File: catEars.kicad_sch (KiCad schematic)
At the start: 32 parts, among them J1 Conn_01x03_Socket, J2 Conn_01x03_Socket, J3 USB_C_Receptacle_PowerOnly_6P, U1 ESP-01v090, U2 AMS1117-3.3

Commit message: pcb
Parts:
- removed C10, C9: 100nF, C0805, symbol Device:C
- removed D10, D9: WS2812B, LED_SMD:LED_WS2812B_PLCC4_5.0x5.0mm_P3.2mm, symbol LED:WS2812B
- removed SW1: ~, symbol Switch:SW_Push
- C1, C11, C12, C2, C3, C4, C5, C6, C7, C8: footprint C0805 -> Capacitor_SMD:C_0805_2012Metric_Pad1.18x1.45mm_HandSolder
- J1, J2: footprint (none) -> Connector_PinHeader_2.54mm:PinHeader_1x03_P2.54mm_Vertical
- R1, R2, R3, R4: footprint 0805 -> Resistor_SMD:R_0805_2012Metric_Pad1.20x1.40mm_HandSolder
- U1: footprint (none) -> ESP8266:ESP-01
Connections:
- net VCC is gone; now on net +5V: J1.2 (Pin_2), J2.2 (Pin_2)
- net LED_out: now also D8.2 (DOUT)
- no-connect marks 0 -> 2

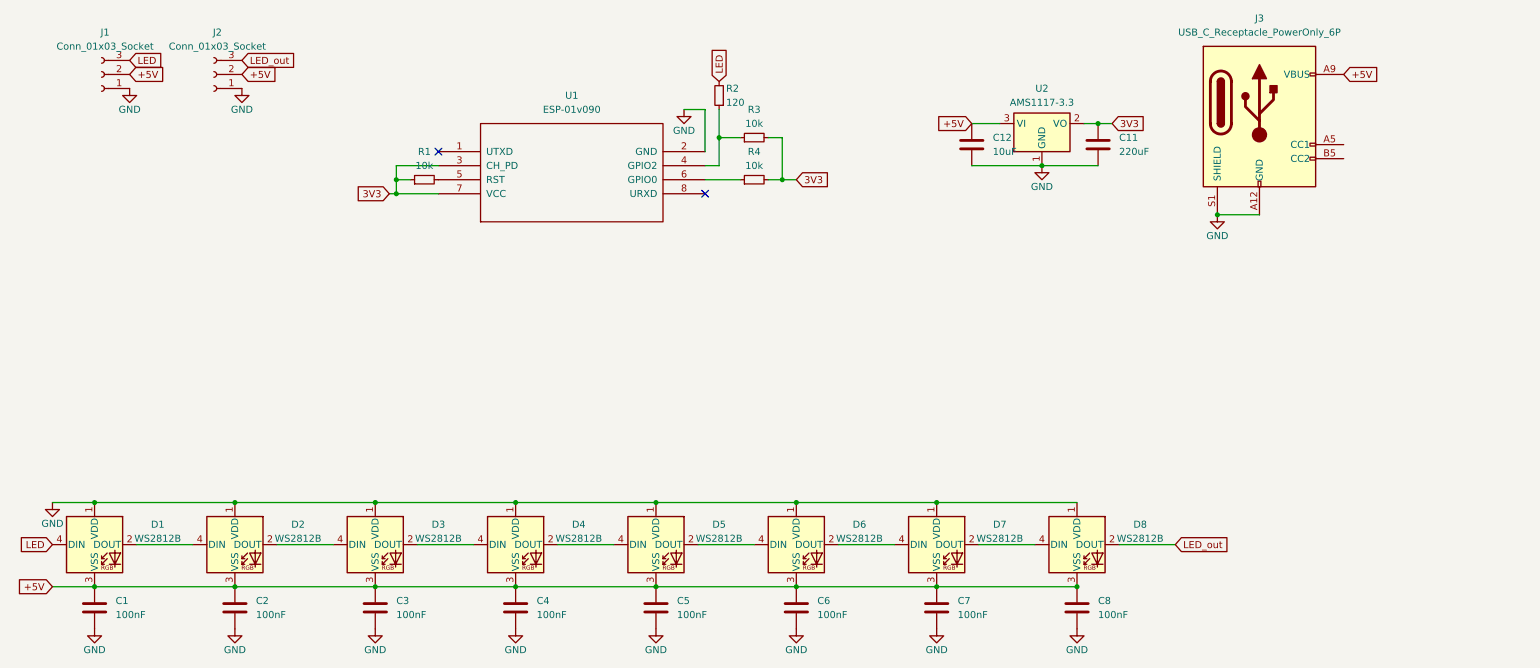
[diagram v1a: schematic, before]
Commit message: fixed WS2812 VSS VDD
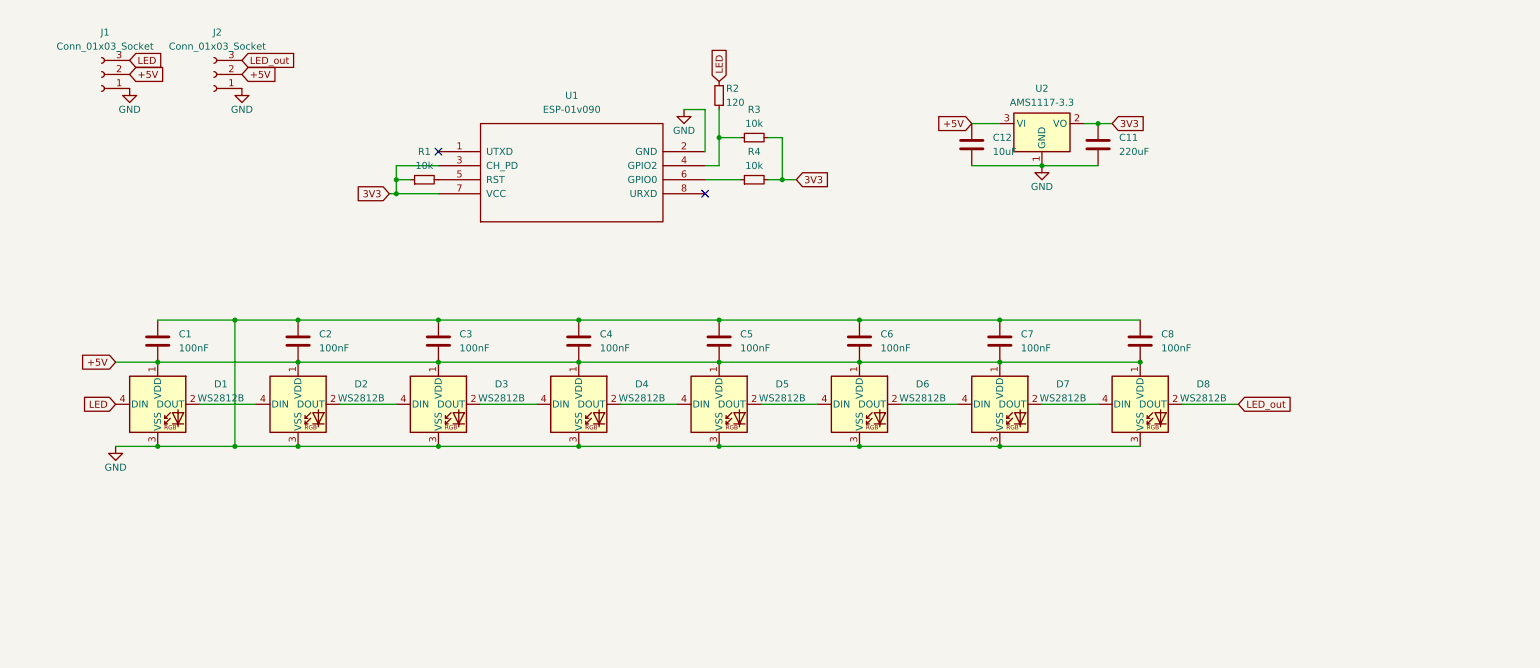
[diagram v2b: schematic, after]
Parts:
- removed J3: USB_C_Receptacle_PowerOnly_6P, symbol Connector:USB_C_Receptacle_PowerOnly_6P
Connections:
- net +5V: now also C1.2, C2.2, C3.2, C4.2, C5.2, C6.2, C7.2, C8.2, D1.1 (VDD), D2.1 (VDD), D3.1 (VDD), D4.1 (VDD), D5.1 (VDD), D6.1 (VDD), D7.1 (VDD), D8.1 (VDD); no longer C1.1, C2.1, C3.1, C4.1, C5.1, C6.1, C7.1, C8.1, D1.3 (VSS), D2.3 (VSS), D3.3 (VSS), D4.3 (VSS), D5.3 (VSS), D6.3 (VSS), D7.3 (VSS), D8.3 (VSS)
- net GND: now also C1.1, C2.1, C3.1, C4.1, C5.1, C6.1, C7.1, C8.1, D1.3 (VSS), D2.3 (VSS), D3.3 (VSS), D4.3 (VSS), D5.3 (VSS), D6.3 (VSS), D7.3 (VSS), D8.3 (VSS); no longer C1.2, C2.2, C3.2, C4.2, C5.2, C6.2, C7.2, C8.2, D1.1 (VDD), D2.1 (VDD), D3.1 (VDD), D4.1 (VDD), D5.1 (VDD), D6.1 (VDD), D7.1 (VDD), D8.1 (VDD)
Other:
- moved on the sheet: D1, D2, D3, D4, D5, D6, D7, D8

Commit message: some optimisations
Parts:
- renumbered R4 to R2, R2 to R4
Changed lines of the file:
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@@
   (symbol (lib_id "Device:R_Small") (at 139.7 33.02 180) (unit 1)
     (in_bom yes) (on_board yes) (dnp no)
-    (property "Reference" "R2" (at 140.97 31.75 0)
+    (property "Reference" "R4" (at 140.97 31.75 0)
       (effects (font (size 1.27 1.27)) (justify right))
     )
@@
       (project "catEars"
         (path "/652ac57d-1a15-486c-917b-0d768241161c"
-          (reference "R2") (unit 1)
+          (reference "R4") (unit 1)
         )
       )
@@
   (symbol (lib_id "Device:R_Small") (at 146.05 48.26 90) (unit 1)
     (in_bom yes) (on_board yes) (dnp no) (fields_autoplaced)
-    (property "Reference" "R4" (at 146.05 43.18 90)
+    (property "Reference" "R2" (at 146.05 43.18 90)
       (effects (font (size 1.27 1.27)))
     )
@@
       (project "catEars"
         (path "/652ac57d-1a15-486c-917b-0d768241161c"
-          (reference "R4") (unit 1)
+          (reference "R2") (unit 1)
         )
       )

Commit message: changed R12 value
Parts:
- C12: value 10uF -> 22uF
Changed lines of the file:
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@@
       (effects (font (size 1.27 1.27)) (justify left))
     )
-    (property "Value" "10uF" (at 189.23 43.18 0)
+    (property "Value" "22uF" (at 189.23 43.18 0)
       (effects (font (size 1.27 1.27)) (justify left))
     )

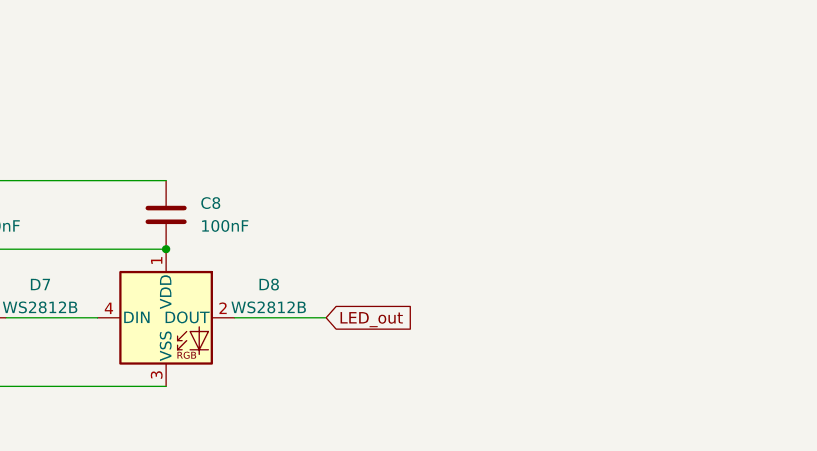
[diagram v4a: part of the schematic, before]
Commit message: added 2 leds in schematic
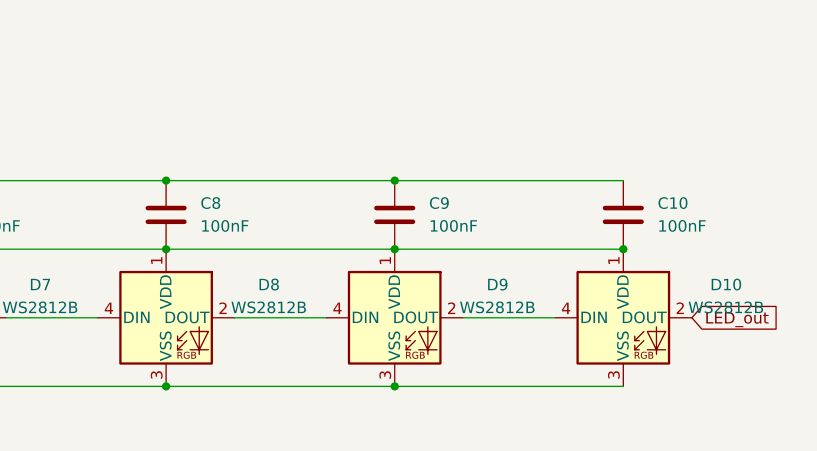
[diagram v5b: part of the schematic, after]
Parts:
- added C10, C9: 100nF, Capacitor_SMD:C_0805_2012Metric_Pad1.18x1.45mm_HandSolder, symbol Device:C
- added D10, D9: WS2812B, LED_SMD:LED_WS2812B_PLCC4_5.0x5.0mm_P3.2mm, symbol LED:WS2812B
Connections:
- net +5V: now also C10.2, C9.2, D10.1 (VDD), D9.1 (VDD)
- net GND: now also C10.1, C9.1, D10.3 (VSS), D9.3 (VSS)
- net LED_out: now also D10.2 (DOUT); no longer D8.2 (DOUT)
- new net: D8.2 (DOUT), D9.4 (DIN)
- new net: D10.4 (DIN), D9.2 (DOUT)
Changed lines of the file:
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@@
   (junction (at 114.3 96.52) (diameter 0) (color 0 0 0 0)
   )
+  (junction (at 241.3 96.52) (diameter 0) (color 0 0 0 0)
+  )
   (junction (at 38.1 96.52) (diameter 0) (color 0 0 0 0)
   )
@@
   (junction (at 139.7 96.52) (diameter 0) (color 0 0 0 0)
   )
+  (junction (at 215.9 96.52) (diameter 0) (color 0 0 0 0)
+  )
   (junction (at 52.07 96.52) (diameter 0) (color 0 0 0 0)
   )
+  (junction (at 88.9 96.52) (diameter 0) (color 0 0 0 0)
+  )
+  (junction (at 63.5 96.52) (diameter 0) (color 0 0 0 0)
+  )
+  (junction (at 139.7 73.66) (diameter 0) (color 0 0 0 0)
+  )
+  (junction (at 208.28 38.1) (diameter 0) (color 194 0 0 1)
+  )
+  (junction (at 198.12 45.72) (diameter 0) (color 0 0 255 1)
+  )
+  (junction (at 114.3 81.28) (diameter 0) (color 132 0 0 1)
+  )
+  (junction (at 215.9 81.28) (diameter 0) (color 0 0 0 0)
+  )
+  (junction (at 266.7 81.28) (diameter 0) (color 0 0 0 0)
+  )
+  (junction (at 63.5 73.66) (diameter 0) (color 0 0 0 0)
+  )
+  (junction (at 139.7 81.28) (diameter 0) (color 132 0 0 1)
+  )
+  (junction (at 190.5 96.52) (diameter 0) (color 0 0 0 0)
+  )
+  (junction (at 241.3 81.28) (diameter 0) (color 132 0 0 1)
+  )
+  (junction (at 165.1 96.52) (diameter 0) (color 0 0 0 0)
+  )
+  (junction (at 190.5 81.28) (diameter 0) (color 132 0 0 1)
+  )
+  (junction (at 215.9 73.66) (diameter 0) (color 0 0 0 0)
+  )
+  (junction (at 165.1 81.28) (diameter 0) (color 132 0 0 1)
+  )
+  (junction (at 139.7 40.64) (diameter 0) (color 0 0 0 0)
+  )
+  (junction (at 88.9 81.28) (diameter 0) (color 132 0 0 1)
+  )
+  (junction (at 165.1 73.66) (diameter 0) (color 0 0 0 0)
+  )
+  (junction (at 52.07 73.66) (diameter 0) (color 0 0 0 0)
+  )
+  (junction (at 241.3 73.66) (diameter 0) (color 0 0 0 0)
+  )
+  (junction (at 63.5 81.28) (diameter 0) (color 132 0 0 1)
+  )
   (junction (at 190.5 73.66) (diameter 0) (color 0 0 0 0)
-  )
-  (junction (at 88.9 96.52) (diameter 0) (color 0 0 0 0)
-  )
-  (junction (at 63.5 96.52) (diameter 0) (color 0 0 0 0)
-  )
-  (junction (at 139.7 73.66) (diameter 0) (color 0 0 0 0)
-  )
-  (junction (at 208.28 38.1) (diameter 0) (color 194 0 0 1)
-  )
-  (junction (at 198.12 45.72) (diameter 0) (color 0 0 255 1)
-  )
-  (junction (at 114.3 81.28) (diameter 0) (color 132 0 0 1)
-  )
-  (junction (at 215.9 81.28) (diameter 0) (color 0 0 0 0)
-  )
-  (junction (at 63.5 73.66) (diameter 0) (color 0 0 0 0)
-  )
-  (junction (at 139.7 81.28) (diameter 0) (color 132 0 0 1)
-  )
-  (junction (at 190.5 96.52) (diameter 0) (color 0 0 0 0)
-  )
-  (junction (at 165.1 96.52) (diameter 0) (color 0 0 0 0)
-  )
-  (junction (at 190.5 81.28) (diameter 0) (color 132 0 0 1)
-  )
-  (junction (at 165.1 81.28) (diameter 0) (color 132 0 0 1)
-  )
-  (junction (at 139.7 40.64) (diameter 0) (color 0 0 0 0)
-  )
-  (junction (at 88.9 81.28) (diameter 0) (color 132 0 0 1)
-  )
-  (junction (at 165.1 73.66) (diameter 0) (color 0 0 0 0)
-  )
-  (junction (at 52.07 73.66) (diameter 0) (color 0 0 0 0)
-  )
-  (junction (at 63.5 81.28) (diameter 0) (color 132 0 0 1)
   )
   (junction (at 88.9 73.66) (diameter 0) (color 0 0 0 0)
@@
     (stroke (width 0) (type default) (color 194 0 0 1))
   )
+  (wire (pts (xy 215.9 81.28) (xy 241.3 81.28))
+    (stroke (width 0) (type default) (color 132 0 0 1))
+  )
   (wire (pts (xy 139.7 45.72) (xy 137.16 45.72))
+    (stroke (width 0) (type default))
+  )
+  (wire (pts (xy 190.5 73.66) (xy 215.9 73.66))
     (stroke (width 0) (type default))
   )
@@
     (stroke (width 0) (type default))
   )
+  (wire (pts (xy 241.3 96.52) (xy 266.7 96.52))
+    (stroke (width 0) (type default) (color 0 0 255 1))
+  )
   (wire (pts (xy 223.52 88.9) (xy 233.68 88.9))
     (stroke (width 0) (type default))
@@
     (stroke (width 0) (type default))
   )
+  (wire (pts (xy 241.3 73.66) (xy 266.7 73.66))
+    (stroke (width 0) (type default) (color 0 0 255 1))
+  )
+  (wire (pts (xy 215.9 96.52) (xy 241.3 96.52))
+    (stroke (width 0) (type default) (color 0 0 255 1))
+  )
   (wire (pts (xy 121.92 88.9) (xy 132.08 88.9))
     (stroke (width 0) (type default))
@@
     (stroke (width 0) (type default) (color 132 0 0 1))
   )
-  (wire (pts (xy 190.5 73.66) (xy 215.9 73.66))
-    (stroke (width 0) (type default) (color 0 0 255 1))
-  )
   (wire (pts (xy 114.3 73.66) (xy 139.7 73.66))
     (stroke (width 0) (type default) (color 0 0 255 1))
@@
     (stroke (width 0) (type default) (color 0 0 255 1))
   )
+  (wire (pts (xy 248.92 88.9) (xy 259.08 88.9))
+    (stroke (width 0) (type default))
+  )
   (wire (pts (xy 114.3 81.28) (xy 139.7 81.28))
     (stroke (width 0) (type default) (color 132 0 0 1))
@@
   (wire (pts (xy 88.9 96.52) (xy 114.3 96.52))
     (stroke (width 0) (type default) (color 0 0 255 1))
+  )
+  (wire (pts (xy 241.3 81.28) (xy 266.7 81.28))
+    (stroke (width 0) (type default) (color 132 0 0 1))
+  )
+  (wire (pts (xy 215.9 73.66) (xy 241.3 73.66))
+    (stroke (width 0) (type default))
   )
   (wire (pts (xy 81.28 48.26) (xy 81.28 45.72))
@@
     )
   )
-  (global_label "LED_out" (shape input) (at 233.68 88.9 0) (fields_autoplaced)
+  (global_label "LED_out" (shape input) (at 274.32 88.9 0) (fields_autoplaced)
     (effects (font (size 1.27 1.27)) (justify left))
-    (property "Intersheetrefs" "${INTERSHEET_REFS}" (at 244.1036 88.9 0)
+    (property "Intersheetrefs" "${INTERSHEET_REFS}" (at 284.7436 88.9 0)
       (effects (font (size 1.27 1.27)) (justify left) hide)
     )
@@
     )
   )
+  (symbol (lib_id "Device:C") (at 241.3 77.47 0) (unit 1)
+    (in_bom yes) (on_board yes) (dnp no) (fields_autoplaced)
+    (property "Reference" "C9" (at 245.11 76.2 0)
+      (effects (font (size 1.27 1.27)) (justify left))
+    )
+    (property "Value" "100nF" (at 245.11 78.74 0)
+      (effects (font (size 1.27 1.27)) (justify left))
+    )
+    (property "Footprint" "Capacitor_SMD:C_0805_2012Metric_Pad1.18x1.45mm_HandSolder" (at 242.2652 81.28 0)
+      (effects (font (size 1.27 1.27)) hide)
+    )
+    (property "Datasheet" "~" (at 241.3 77.47 0)
+      (effects (font (size 1.27 1.27)) hide)
+    )
+    (pin "1")
+    (pin "2")
+    (instances
+      (project "catEars"
+        (path "/652ac57d-1a15-486c-917b-0d768241161c"
+          (reference "C9") (unit 1)
+        )
+      )
+    )
+  )
   (symbol (lib_id "Device:C") (at 63.5 77.47 0) (unit 1)
     (in_bom yes) (on_board yes) (dnp no) (fields_autoplaced)
@@
     )
   )
+  (symbol (lib_id "LED:WS2812B") (at 266.7 88.9 0) (unit 1)
+    (in_bom yes) (on_board yes) (dnp no) (fields_autoplaced)
+    (property "Reference" "D10" (at 278.13 85.2521 0)
+      (effects (font (size 1.27 1.27)))
+    )
+    (property "Value" "WS2812B" (at 278.13 87.7921 0)
+      (effects (font (size 1.27 1.27)))
+    )
+    (property "Footprint" "LED_SMD:LED_WS2812B_PLCC4_5.0x5.0mm_P3.2mm" (at 267.97 96.52 0)
+      (effects (font (size 1.27 1.27)) (justify left top) hide)
+    )
+    (property "Datasheet" "https://cdn-shop.adafruit.com/datasheets/WS2812B.pdf" (at 269.24 98.425 0)
+      (effects (font (size 1.27 1.27)) (justify left top) hide)
+    )
+    (pin "1")
+    (pin "3")
+    (pin "2")
+    (pin "4")
+    (instances
+      (project "catEars"
+        (path "/652ac57d-1a15-486c-917b-0d768241161c"
+          (reference "D10") (unit 1)
+        )
+      )
+    )
+  )
   (symbol (lib_id "Device:R_Small") (at 146.05 40.64 90) (unit 1)
     (in_bom yes) (on_board yes) (dnp no) (fields_autoplaced)
@@
     )
   )
+  (symbol (lib_id "LED:WS2812B") (at 241.3 88.9 0) (unit 1)
+    (in_bom yes) (on_board yes) (dnp no) (fields_autoplaced)
+    (property "Reference" "D9" (at 252.73 85.2521 0)
+      (effects (font (size 1.27 1.27)))
+    )
+    (property "Value" "WS2812B" (at 252.73 87.7921 0)
+      (effects (font (size 1.27 1.27)))
+    )
+    (property "Footprint" "LED_SMD:LED_WS2812B_PLCC4_5.0x5.0mm_P3.2mm" (at 242.57 96.52 0)
+      (effects (font (size 1.27 1.27)) (justify left top) hide)
+    )
+    (property "Datasheet" "https://cdn-shop.adafruit.com/datasheets/WS2812B.pdf" (at 243.84 98.425 0)
+      (effects (font (size 1.27 1.27)) (justify left top) hide)
+    )
+    (pin "1")
+    (pin "3")
+    (pin "2")
+    (pin "4")
+    (instances
+      (project "catEars"
+        (path "/652ac57d-1a15-486c-917b-0d768241161c"
+          (reference "D9") (unit 1)
+        )
+      )
+    )
+  )
   (symbol (lib_id "LED:WS2812B") (at 139.7 88.9 0) (unit 1)
     (in_bom yes) (on_board yes) (dnp no) (fields_autoplaced)
@@
         )
       )
+    )
+  )
+  (symbol (lib_id "Device:C") (at 266.7 77.47 0) (unit 1)
+    (in_bom yes) (on_board yes) (dnp no) (fields_autoplaced)
+    (property "Reference" "C10" (at 270.51 76.2 0)
+      (effects (font (size 1.27 1.27)) (justify left))
+    )
+    (property "Value" "100nF" (at 270.51 78.74 0)
+      (effects (font (size 1.27 1.27)) (justify left))
+    )
+    (property "Footprint" "Capacitor_SMD:C_0805_2012Metric_Pad1.18x1.45mm_HandSolder" (at 267.6652 81.28 0)
+      (effects (font (size 1.27 1.27)) hide)
+    )
+    (property "Datasheet" "~" (at 266.7 77.47 0)
+      (effects (font (size 1.27 1.27)) hide)
+    )
+    (pin "1")
+    (pin "2")
+    (instances
+      (project "catEars"
+        (path "/652ac57d-1a15-486c-917b-0d768241161c"
+          (reference "C10") (unit 1)
+        )
+      )

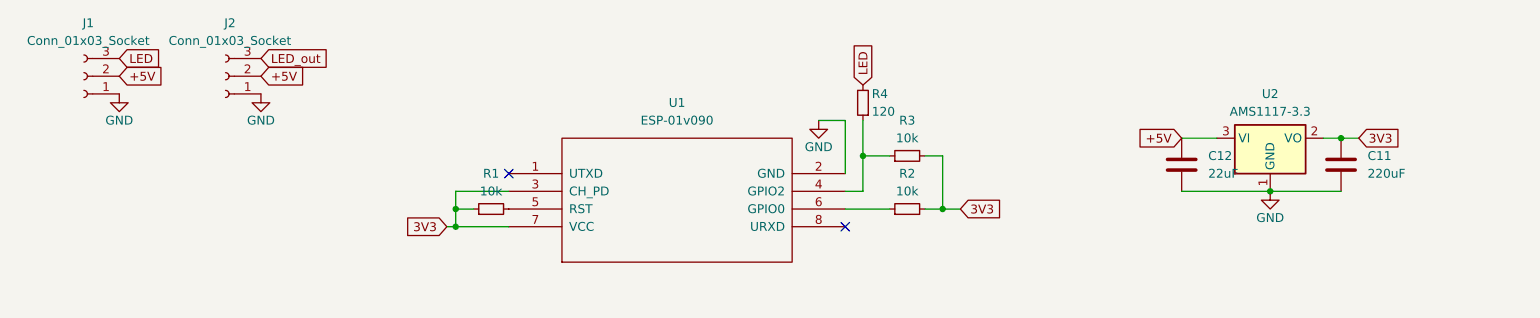
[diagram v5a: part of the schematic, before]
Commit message: changed C11 value
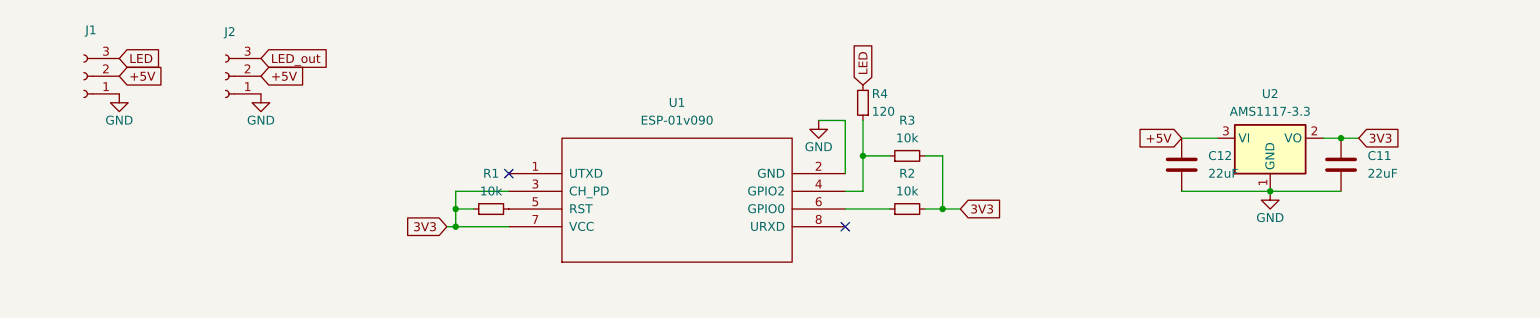
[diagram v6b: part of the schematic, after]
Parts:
- C11: value 220uF -> 22uF
- J1, J2: value Conn_01x03_Socket -> ~
